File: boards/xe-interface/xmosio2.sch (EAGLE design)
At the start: 122 parts, among them IC1 IDTQS3245QSOP20, IC2 IDTQS3245QSOP20, IC3 IDTQS3245QSOP20, IC4 IDTQS3245QSOP20, IC5 IDTQS3245QSOP20, J1 SD_CARD, U1 24 MHz Osc. (F535L-24), X1 0446200002

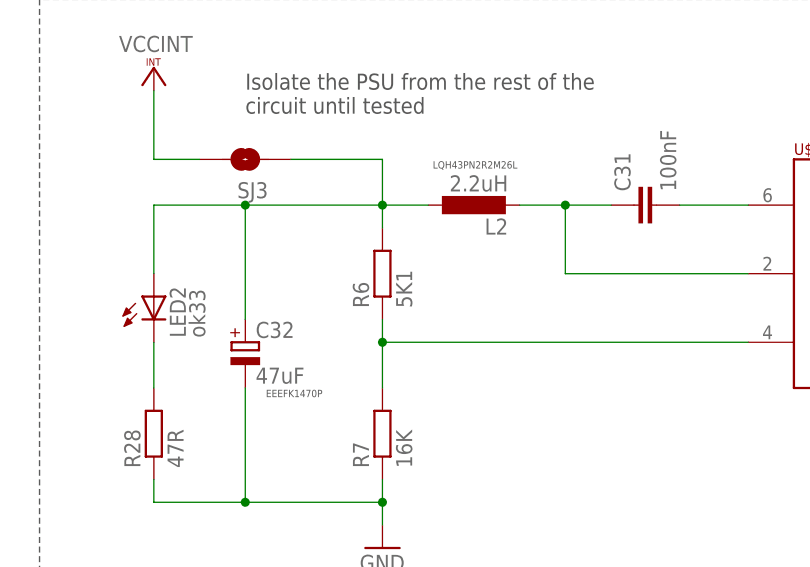
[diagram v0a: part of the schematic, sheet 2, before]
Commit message: Change the resistor value in the 1v power supply to 3.9k from 5.1k, which provides a better 1v supply.
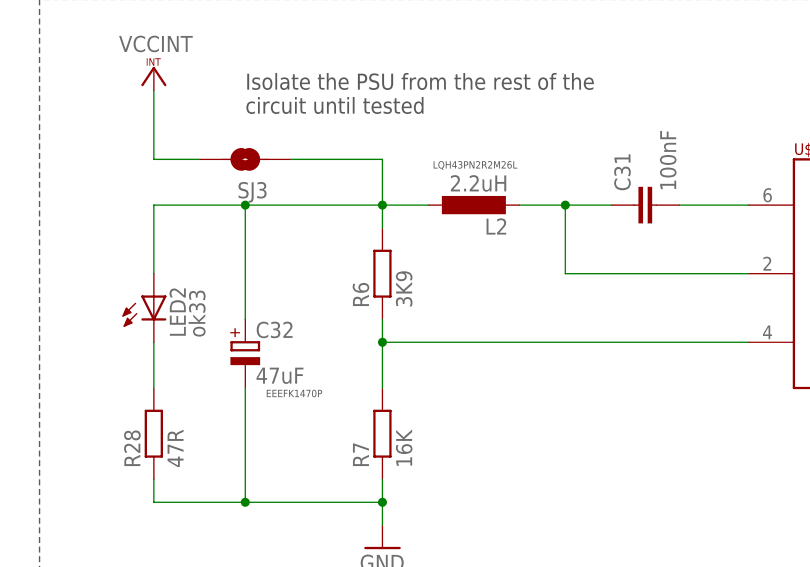
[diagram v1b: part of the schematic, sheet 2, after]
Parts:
- R6: value 5K1 -> 3K9
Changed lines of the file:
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@@
 <part name="L2" library="rcl" deviceset="L-EU" device="L1812" value="2.2uH"/>
 <part name="C31" library="rcl" deviceset="C-EU" device="C1206" value="100nF"/>
-<part name="R6" library="rcl" deviceset="R-EU_" device="R1206" value="5K1"/>
+<part name="R6" library="rcl" deviceset="R-EU_" device="R1206" value="3K9"/>
 <part name="R7" library="rcl" deviceset="R-EU_" device="R1206" value="16K"/>
 <part name="GND23" library="supply1" deviceset="GND" device=""/>
